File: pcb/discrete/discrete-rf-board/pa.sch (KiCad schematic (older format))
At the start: 0 parts

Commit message: Design DAC/ADC stages, pass out all control signals to top sheet
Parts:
- added C? (x6): 100 pF RF, symbol Device:C_Small
- added C?: 3.0 pF RF, symbol Device:C_Small
- added C?: 5.45 pF RF, symbol Device:C_Small
- added C? (x3): 1 nF, symbol Device:C_Small
- added J? (x3): Conn_Coaxial, symbol Connector:Conn_Coaxial
- added L?: 10.0 nH, symbol Device:L_Small
- added L?: 9.5 nH, symbol Device:L_Small
- added L?: 220 nH, symbol Device:L_Small
- added Q?: Q_NPN_BCEE, symbol discrete-parts:Q_NPN_BCEE
- added R?: 75R, symbol Device:R_Small
- added R?: 8k2R, symbol Device:R_Small
- added R?: 22R, symbol Device:R_Small
- added R?: 1k8R, symbol Device:R_Small
- added R? (x3): 0R, symbol Device:R_Small
- added R? (x2): DNP 0402, symbol Device:R_Small
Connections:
- new net: C?.1, R?.1
- new net: J?.1 (In), L?.1, L?.2, Q?.2 (C), R?.2
- new net: C?.2, R?.2
- new net: J?.1 (In), L?.2, Q?.1 (B), R?.1, R?.2
- new net: C?.1, C?.1, C?.1, C?.1, L?.1, R?.2, R?.2
- new net: C?.1, L?.2, R?.1
- new net: C?.1, R?.1, R?.2
- new net: C?.2, R?.1
- new net: C?.1, L?.1, R?.2
- new net +5V0: C?.1, C?.1, R?.1
- new net GND: C?.2, C?.2, C?.2, C?.2, C?.2, C?.2, C?.2, C?.2, C?.2, J?.2 (Ext), J?.2 (Ext), J?.2 (Ext), Q?.3 (E), Q?.4 (C), R?.1, R?.2, R?.2
- new net IN: J?.1 (In), R?.1, R?.1
- new net OUT: C?.1
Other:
- note added: "TODO make sure the matching circuit values are\ncalculated for Vce=5V"
- note added: "Vbe=~~0.827V, ib=~~0.05mA, ic=5mA\nNF=1.5 dB, K=~~16dB"

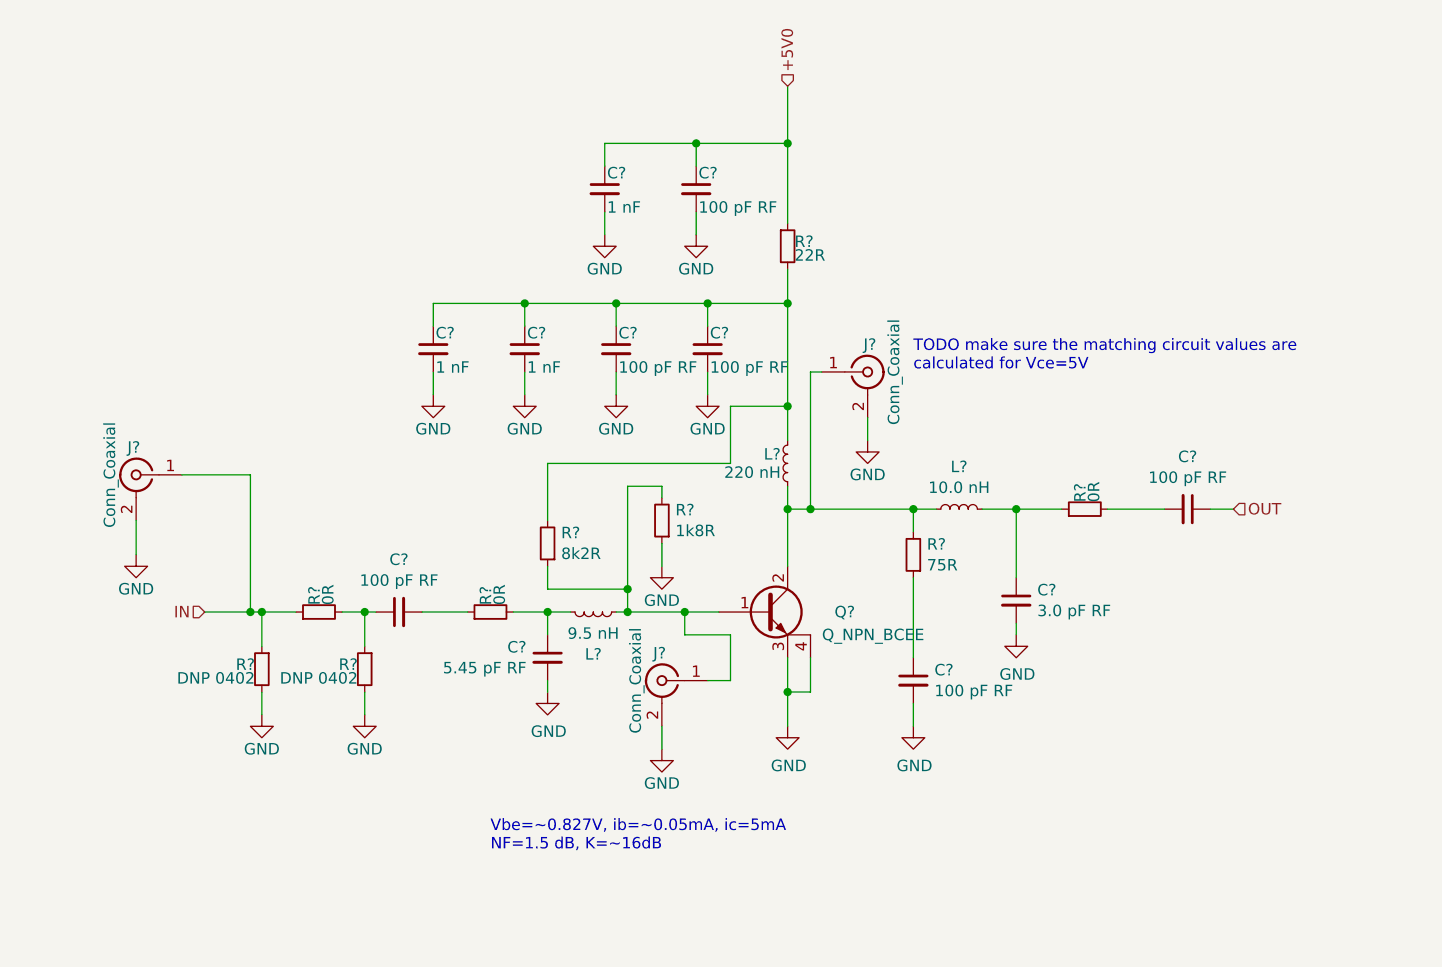
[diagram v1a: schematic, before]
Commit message: Wire out all control signals to connectors TODO PLL charge pump loop, bypass caps in attenuator circuit, antialiasing filter for ADC frontend
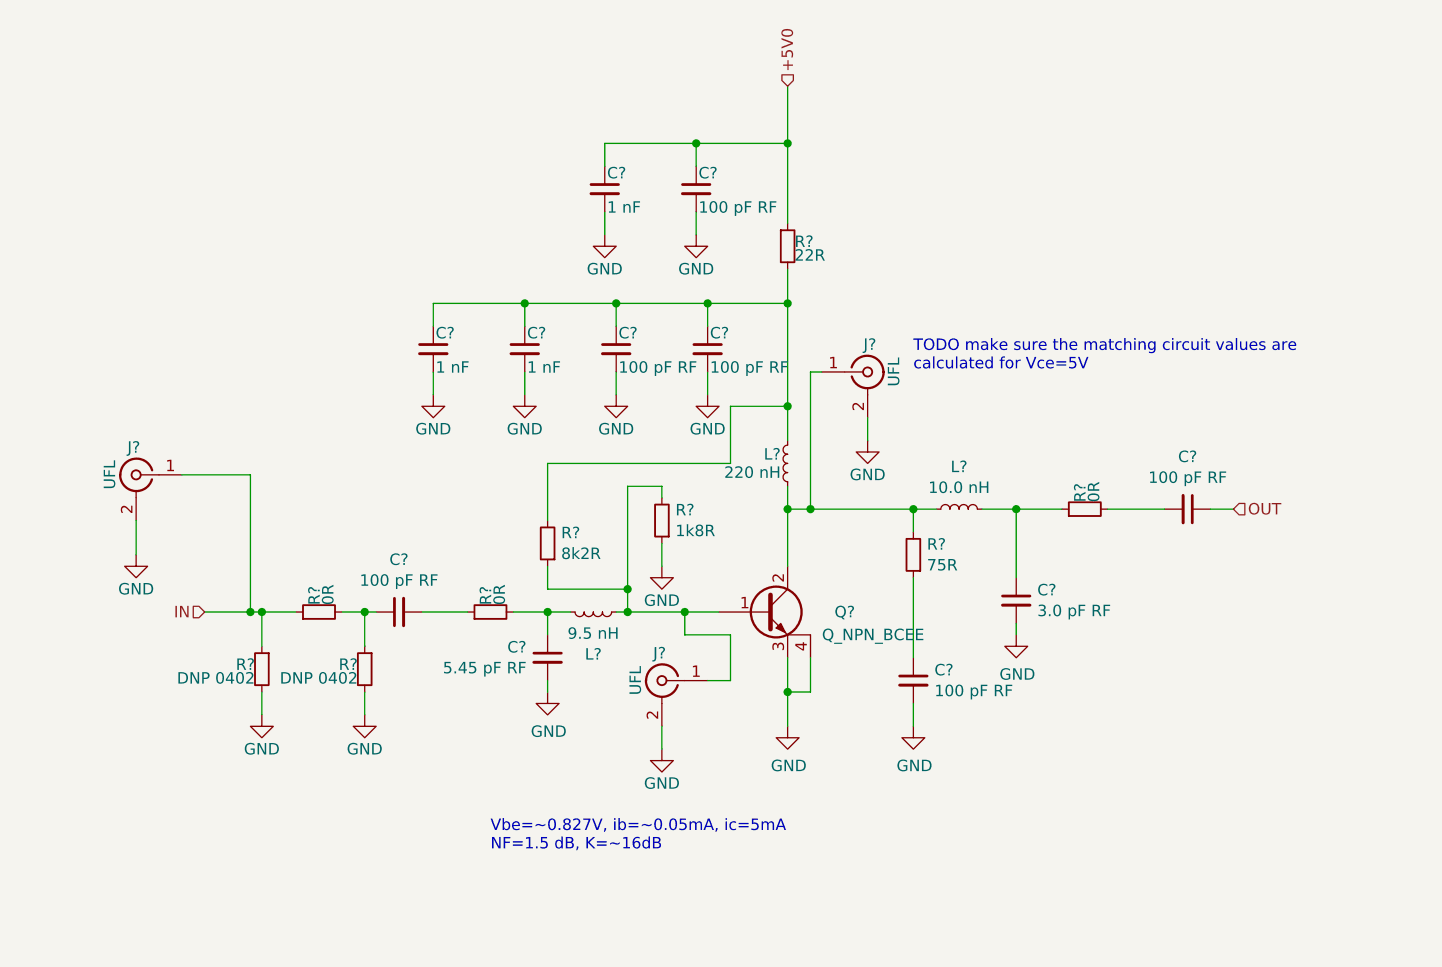
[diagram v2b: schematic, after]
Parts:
- J? (x3): value Conn_Coaxial -> UFL
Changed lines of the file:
@@
 AR Path="/5CA6B0B3/5D830BD7/5D91A9B1" Ref="J?"  Part="1"
 F 0 "J?" H 6010 3320 50  0000 C CNN
-F 1 "Conn_Coaxial" V 6115 3200 50  0000 C CNN
+F 1 "UFL" V 6115 3200 50  0000 C CNN
 F 2 "" H 6000 3200 50  0001 C CNN
 F 3 " ~" H 6000 3200 50  0001 C CNN
@@
 AR Path="/5CA6B0B3/5D830BD7/5D91A9B7" Ref="J?"  Part="1"
 F 0 "J?" H 5110 4670 50  0000 C CNN
-F 1 "Conn_Coaxial" V 5215 4550 50  0000 C CNN
+F 1 "UFL" V 5215 4550 50  0000 C CNN
 F 2 "" H 5100 4550 50  0001 C CNN
 F 3 " ~" H 5100 4550 50  0001 C CNN
@@
 AR Path="/5CA6B0B3/5D830BD7/5D92AD9B" Ref="J?"  Part="1"
 F 0 "J?" H 2810 3770 50  0000 C CNN
-F 1 "Conn_Coaxial" V 2915 3650 50  0000 C CNN
+F 1 "UFL" V 2915 3650 50  0000 C CNN
 F 2 "" H 2800 3650 50  0001 C CNN
 F 3 " ~" H 2800 3650 50  0001 C CNN

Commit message: Add matching PNP/NPN transistor pairs, fix pin numbering for BFU520R transistors TODO fix biasing on power stage, source last NPN transistor, autofill and start sourcing passives
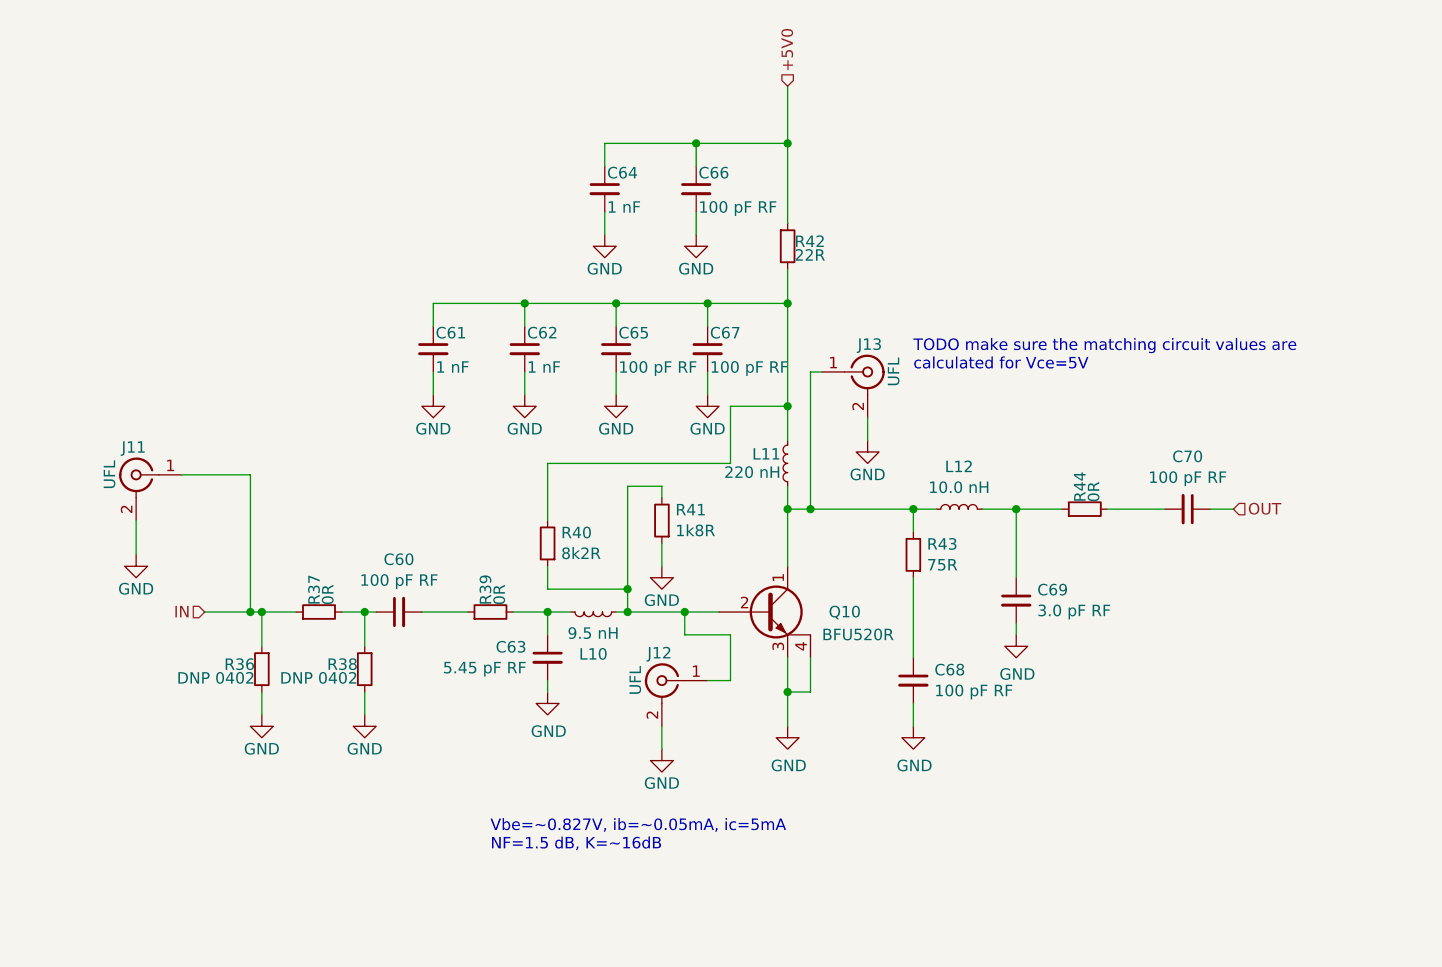
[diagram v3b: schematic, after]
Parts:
- removed Q?: Q_NPN_BCEE, symbol discrete-parts:Q_NPN_BCEE
- added Q10: BFU520R, discrete_footprints:NXP_SOT143B, symbol discrete-parts:Q_NPN_CBEE
- gave numbers to parts that had none: 26
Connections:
- net GND: now also Q10.3 (E), Q10.4 (C)
- net at J13.1 (In), L11.2, L12.1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: now also Q10.1 (C)
- net at J12.1 (In), L10.2, R40.1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: now also Q10.2 (B)

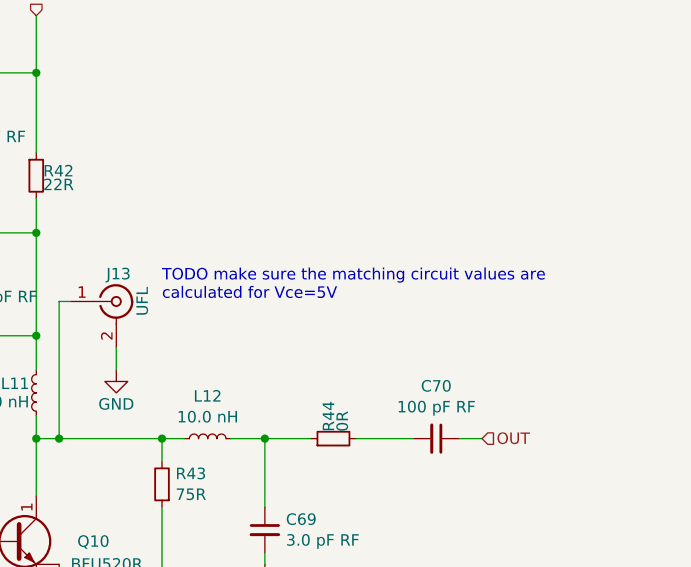
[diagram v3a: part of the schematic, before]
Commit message: All component values set (TODO change transistor gain stages to match values from experimentation
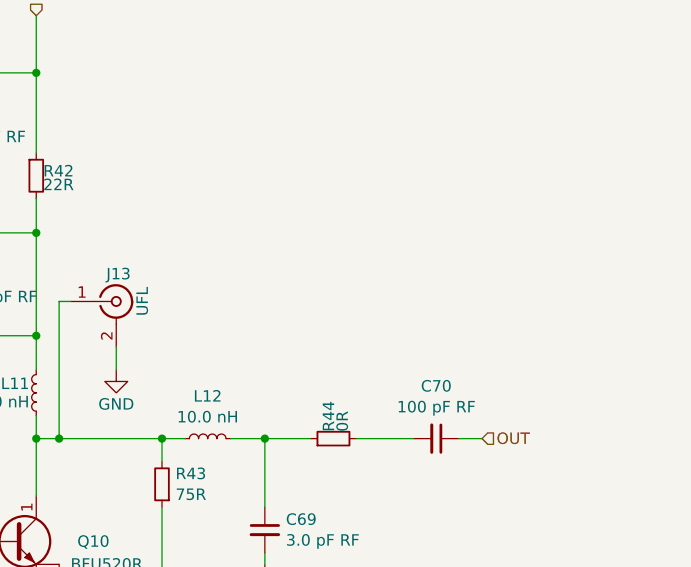
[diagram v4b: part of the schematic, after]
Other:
- note removed: "TODO make sure the matching circuit values are\ncalculated for Vce=5V"
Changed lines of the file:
@@
 Text Notes 4350 5300 0    50   ~ 0
 Vbe=~~0.827V, ib=~~0.05mA, ic=5mA\nNF=1.5 dB, K=~~16dB
-Text Notes 6200 3200 0    50   ~ 0
-TODO make sure the matching circuit values are\ncalculated for Vce=5V
 $Comp
 L Device:C_Small C?

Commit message: Autofill; lots left to do
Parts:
- J11, J12, J13: footprint (none) -> discrete_footprints:2337019-1; Mouser (none) -> 571-2337019-1
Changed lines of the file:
@@
 F 0 "J13" H 6010 3320 50  0000 C CNN
 F 1 "UFL" V 6115 3200 50  0000 C CNN
-F 2 "" H 6000 3200 50  0001 C CNN
+F 2 "discrete_footprints:2337019-1" H 6000 3200 50  0001 C CNN
 F 3 " ~" H 6000 3200 50  0001 C CNN
+F 4 " 571-2337019-1" H 6000 3200 50  0001 C CNN "Mouser"
 	1    6000 3200
 	1    0    0    -1
@@
 F 0 "J12" H 5110 4670 50  0000 C CNN
 F 1 "UFL" V 5215 4550 50  0000 C CNN
-F 2 "" H 5100 4550 50  0001 C CNN
+F 2 "discrete_footprints:2337019-1" H 5100 4550 50  0001 C CNN
 F 3 " ~" H 5100 4550 50  0001 C CNN
+F 4 " 571-2337019-1" H 5100 4550 50  0001 C CNN "Mouser"
 	1    5100 4550
 	-1   0    0    -1
@@
 F 0 "J11" H 2810 3770 50  0000 C CNN
 F 1 "UFL" V 2915 3650 50  0000 C CNN
-F 2 "" H 2800 3650 50  0001 C CNN
+F 2 "discrete_footprints:2337019-1" H 2800 3650 50  0001 C CNN
 F 3 " ~" H 2800 3650 50  0001 C CNN
+F 4 " 571-2337019-1" H 2800 3650 50  0001 C CNN "Mouser"
 	1    2800 3650
 	-1   0    0    -1

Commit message: Autofill
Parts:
- C60, C65, C66, C67, C68, C70: footprint (none) -> Capacitor_SMD:C_0402_1005Metric; Mouser (none) -> 791-RF15N101J250CT
- R37, R39, R44: footprint (none) -> Capacitor_SMD:C_0402_1005Metric; Mouser (none) -> 71-CRCW04020000Z0EDC
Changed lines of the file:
@@
 F 0 "C70" V 7629 3800 50  0000 C CNN
 F 1 "100 pF RF" V 7538 3800 50  0000 C CNN
-F 2 "" H 7400 3800 50  0001 C CNN
+F 2 "Capacitor_SMD:C_0402_1005Metric" H 7400 3800 50  0001 C CNN
 F 3 "~" H 7400 3800 50  0001 C CNN
+F 4 "791-RF15N101J250CT " H 7400 3800 50  0001 C CNN "Mouser"
 	1    7400 3800
 	0    1    -1   0
@@
 F 0 "C60" V 4179 4250 50  0000 C CNN
 F 1 "100 pF RF" V 4088 4250 50  0000 C CNN
-F 2 "" H 3950 4250 50  0001 C CNN
+F 2 "Capacitor_SMD:C_0402_1005Metric" H 3950 4250 50  0001 C CNN
 F 3 "~" H 3950 4250 50  0001 C CNN
+F 4 "791-RF15N101J250CT " H 3950 4250 50  0001 C CNN "Mouser"
 	1    3950 4250
 	0    -1   -1   0
@@
 F 0 "C65" H 4910 3170 50  0000 L CNN
 F 1 "100 pF RF" H 4910 3020 50  0000 L CNN
-F 2 "" H 4900 3100 50  0001 C CNN
+F 2 "Capacitor_SMD:C_0402_1005Metric" H 4900 3100 50  0001 C CNN
 F 3 "~" H 4900 3100 50  0001 C CNN
+F 4 "791-RF15N101J250CT " H 4900 3100 50  0001 C CNN "Mouser"
 	1    4900 3100
 	1    0    0    -1
@@
 F 0 "C67" H 5310 3170 50  0000 L CNN
 F 1 "100 pF RF" H 5310 3020 50  0000 L CNN
-F 2 "" H 5300 3100 50  0001 C CNN
+F 2 "Capacitor_SMD:C_0402_1005Metric" H 5300 3100 50  0001 C CNN
 F 3 "~" H 5300 3100 50  0001 C CNN
+F 4 "791-RF15N101J250CT " H 5300 3100 50  0001 C CNN "Mouser"
 	1    5300 3100
 	1    0    0    -1
@@
 F 0 "C66" H 5260 2470 50  0000 L CNN
 F 1 "100 pF RF" H 5260 2320 50  0000 L CNN
-F 2 "" H 5250 2400 50  0001 C CNN
+F 2 "Capacitor_SMD:C_0402_1005Metric" H 5250 2400 50  0001 C CNN
 F 3 "~" H 5250 2400 50  0001 C CNN
+F 4 "791-RF15N101J250CT " H 5250 2400 50  0001 C CNN "Mouser"
 	1    5250 2400
 	1    0    0    -1
@@
 F 0 "C68" H 6292 4596 50  0000 L CNN
 F 1 "100 pF RF" H 6292 4505 50  0000 L CNN
-F 2 "" H 6200 4550 50  0001 C CNN
+F 2 "Capacitor_SMD:C_0402_1005Metric" H 6200 4550 50  0001 C CNN
 F 3 "~" H 6200 4550 50  0001 C CNN
+F 4 "791-RF15N101J250CT " H 6200 4550 50  0001 C CNN "Mouser"
 	1    6200 4550
 	1    0    0    -1
@@
 F 0 "R37" H 3630 4270 50  0000 L CNN
 F 1 "0R" H 3630 4210 50  0000 L CNN
-F 2 "" H 3600 4250 50  0001 C CNN
+F 2 "Capacitor_SMD:C_0402_1005Metric" H 3600 4250 50  0001 C CNN
 F 3 "~" H 3600 4250 50  0001 C CNN
+F 4 "71-CRCW04020000Z0EDC" H 3600 4250 50  0001 C CNN "Mouser"
 	1    3600 4250
 	0    -1   -1   0
@@
 F 0 "R39" H 4380 4270 50  0000 L CNN
 F 1 "0R" H 4380 4210 50  0000 L CNN
-F 2 "" H 4350 4250 50  0001 C CNN
+F 2 "Capacitor_SMD:C_0402_1005Metric" H 4350 4250 50  0001 C CNN
 F 3 "~" H 4350 4250 50  0001 C CNN
+F 4 "71-CRCW04020000Z0EDC" H 4350 4250 50  0001 C CNN "Mouser"
 	1    4350 4250
 	0    -1   -1   0
@@
 F 0 "R44" H 6980 3820 50  0000 L CNN
 F 1 "0R" H 6980 3760 50  0000 L CNN
-F 2 "" H 6950 3800 50  0001 C CNN
+F 2 "Capacitor_SMD:C_0402_1005Metric" H 6950 3800 50  0001 C CNN
 F 3 "~" H 6950 3800 50  0001 C CNN
+F 4 "71-CRCW04020000Z0EDC" H 6950 3800 50  0001 C CNN "Mouser"
 	1    6950 3800
 	0    -1   -1   0
